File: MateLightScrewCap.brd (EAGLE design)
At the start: 24 x 24 mm, 3 parts, among them X1 PHOENIX-1778780, X3 PHOENIX-1778780

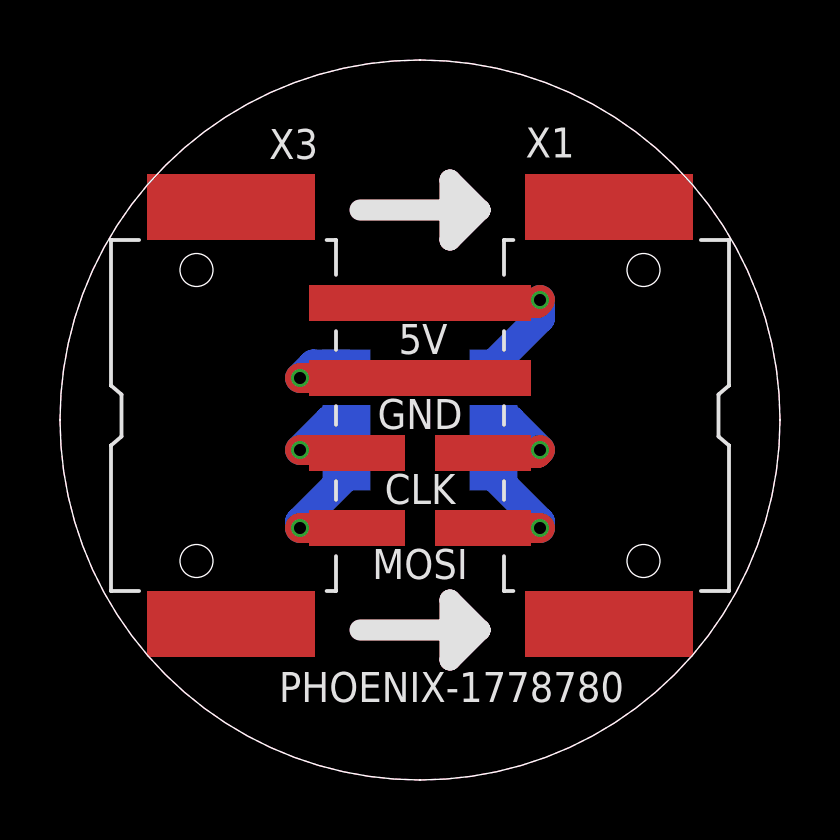
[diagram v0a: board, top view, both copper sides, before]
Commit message: Connector getauscht: Phoenix-1778780 → JST S4B-PH-SM4-TB
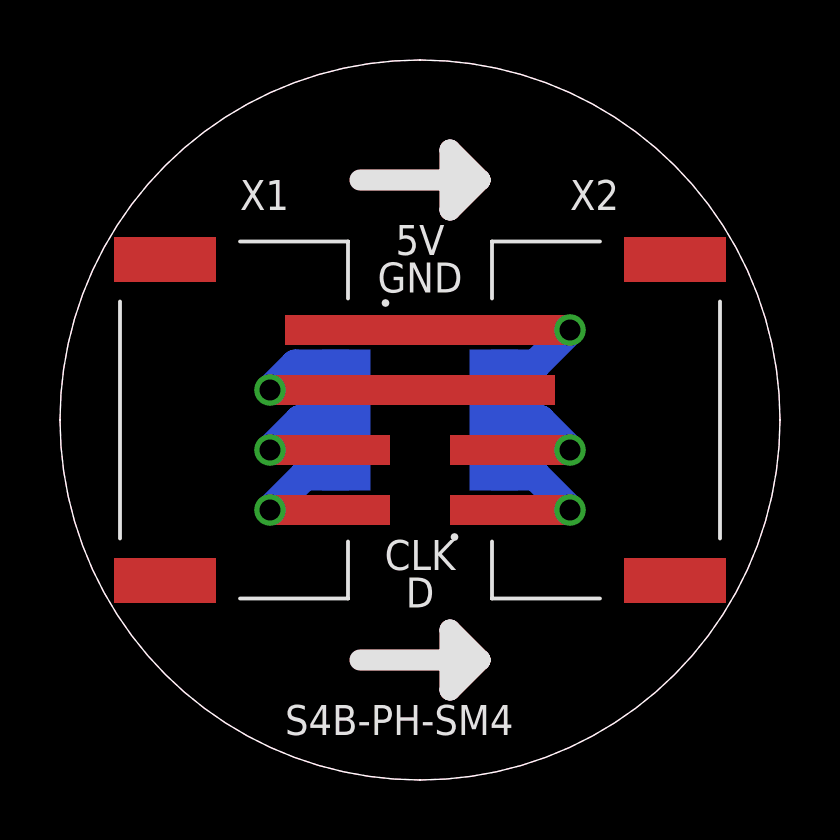
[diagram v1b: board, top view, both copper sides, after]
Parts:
- removed X3: PHOENIX-1778780, h8-conector:PHOENIX-1778780
- added X2: S4B-PH-SM4, h8-connector:JST_S4B-PH-SM4-TB
- X1: value PHOENIX-1778780 -> S4B-PH-SM4-TB; device h8-conector:PHOENIX-1778780 -> h8-connector:JST_S4B-PH-SM4-TB
- moved X1 21.1 mm to (-10.0, 0.00)
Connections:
- removed net LED-SPI-CLK: LD1.2, X3.3
- removed net LED-SPI-MOSI: LD1.1, X3.4
- removed net N$37: LD1.5, X1.2
- removed net N$39: LD1.4, X1.1
- new net LED-SPI-CLK-IN: LD1.2, X1.3
- new net LED-SPI-CLK-OUT: LD1.5, X2.2
- new net LED-SPI-MOSI-IN: LD1.1, X1.4
- new net LED-SPI-MOSI-OUT: LD1.4, X2.1
- net +5V: now also X1.1, X2.4; no longer X1.4, X3.1
- net GND: now also X1.2, X2.3; no longer X1.3, X3.2
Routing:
- net LED-SPI-MOSI-OUT: track 0.00 -> 5.28 mm, vias 0 -> 1
- net LED-SPI-MOSI-IN: track 0.00 -> 5.28 mm, vias 0 -> 1
- net LED-SPI-CLK-OUT: track 0.00 -> 5.21 mm, vias 0 -> 1
- net LED-SPI-CLK-IN: track 0.00 -> 5.21 mm, vias 0 -> 1
- net N$39: track 4.29 -> 0.00 mm, vias 1 -> 0
- net LED-SPI-MOSI: track 4.29 -> 0.00 mm, vias 1 -> 0
- net N$37: track 3.91 -> 0.00 mm, vias 1 -> 0
- net LED-SPI-CLK: track 3.91 -> 0.00 mm, vias 1 -> 0
- net GND: track 7.84 -> 10.7 mm
- net +5V: track 8.93 -> 10.8 mm
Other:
- board text added: "D"
- board text added: "MIT License MateLightScrewCap by Hans Achterbahn 31.10.2019 v0.1.0"
- board text removed: "MIT License MateLightScrewCap by Hans Achterbahn 26.10.2019 v0.1.0"
- board text removed: "MOSI"

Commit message: Repaired document consistency | correct current source properties
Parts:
- X1: value S4B-PH-SM4-TB -> S4B-PH-SM4
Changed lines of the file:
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@@
 <attribute name="VALUE" x="-4.5" y="-10.5" size="1" layer="25" font="vector"/>
 </element>
-<element name="X1" library="h8-connector" library_urn="urn:adsk.eagle:library:13329207" package="JST_S4B-PH-SM4-TB" package3d_urn="urn:adsk.eagle:package:14877512/5" value="S4B-PH-SM4-TB" x="-10" y="0" smashed="yes" rot="R90">
+<element name="X1" library="h8-connector" library_urn="urn:adsk.eagle:library:13329207" package="JST_S4B-PH-SM4-TB" package3d_urn="urn:adsk.eagle:package:14877512/5" value="S4B-PH-SM4" x="-10" y="0" smashed="yes" rot="R90">
 <attribute name="DESCRIPTION" value=" Socket; wire-board; male; PIN: 4; 2mm; SMT; PH; 100V; 2A; -25÷85°C " x="-10" y="0" size="1.778" layer="27" rot="R90" display="off"/>
 <attribute name="DIGI-KEY" value="455-1751-2-ND" x="-10" y="0" size="1.778" layer="27" rot="R90" display="off"/>

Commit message: Konsistenzfehler behoben
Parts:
- X1: value S4B-PH-SM4 -> S4B-PH-SM4-TB
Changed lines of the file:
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@@
 <attribute name="VALUE" x="-4.5" y="-10.5" size="1" layer="25" font="vector"/>
 </element>
-<element name="X1" library="h8-connector" library_urn="urn:adsk.eagle:library:13329207" package="JST_S4B-PH-SM4-TB" package3d_urn="urn:adsk.eagle:package:14877512/5" value="S4B-PH-SM4" x="-10" y="0" smashed="yes" rot="R90">
+<element name="X1" library="h8-connector" library_urn="urn:adsk.eagle:library:13329207" package="JST_S4B-PH-SM4-TB" package3d_urn="urn:adsk.eagle:package:14877512/5" value="S4B-PH-SM4-TB" x="-10" y="0" smashed="yes" rot="R90">
 <attribute name="DESCRIPTION" value=" Socket; wire-board; male; PIN: 4; 2mm; SMT; PH; 100V; 2A; -25÷85°C " x="-10" y="0" size="1.778" layer="27" rot="R90" display="off"/>
 <attribute name="DIGI-KEY" value="455-1751-2-ND" x="-10" y="0" size="1.778" layer="27" rot="R90" display="off"/>
